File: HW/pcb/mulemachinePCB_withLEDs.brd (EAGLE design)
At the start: 90.2 x 52.1 mm, 29 parts, among them IC1 LD117AV50, IC2 MEGA8-P, J1 DCJ0202, Q1 16Mhz

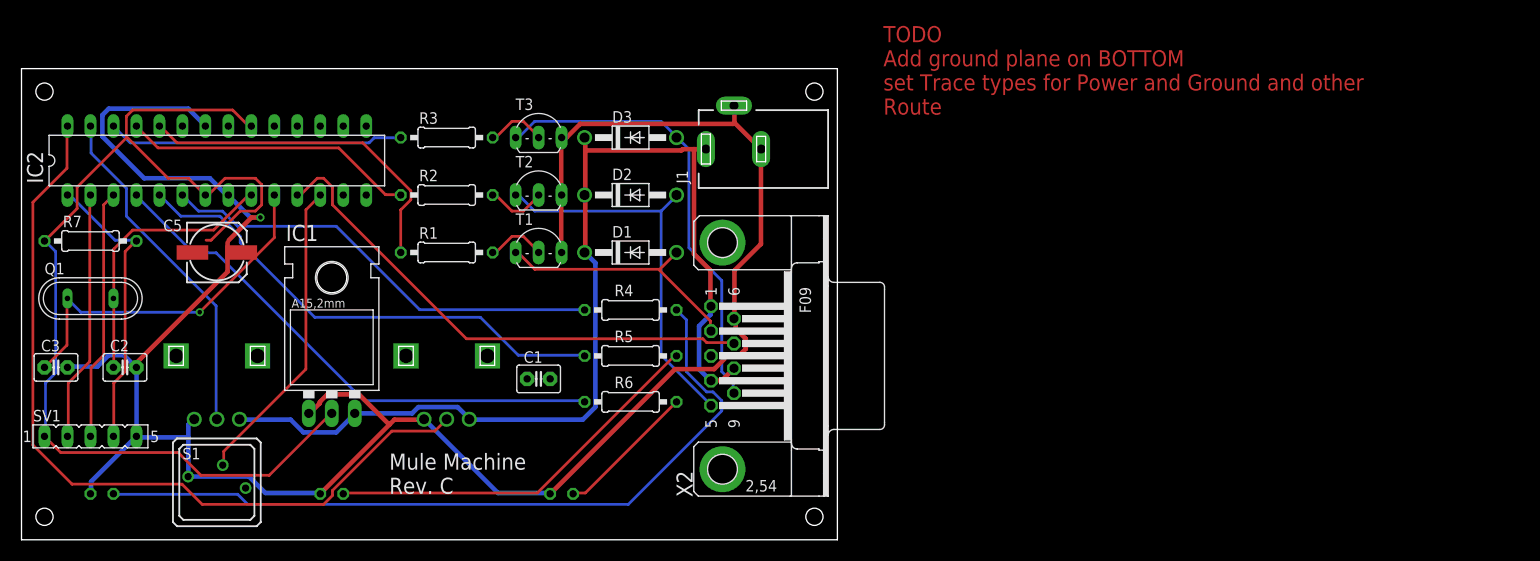
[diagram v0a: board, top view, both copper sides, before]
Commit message: finished layout for PCB. implemented trace widths for PWR and GND. Lined up hole placement to match with Front panel laser design.
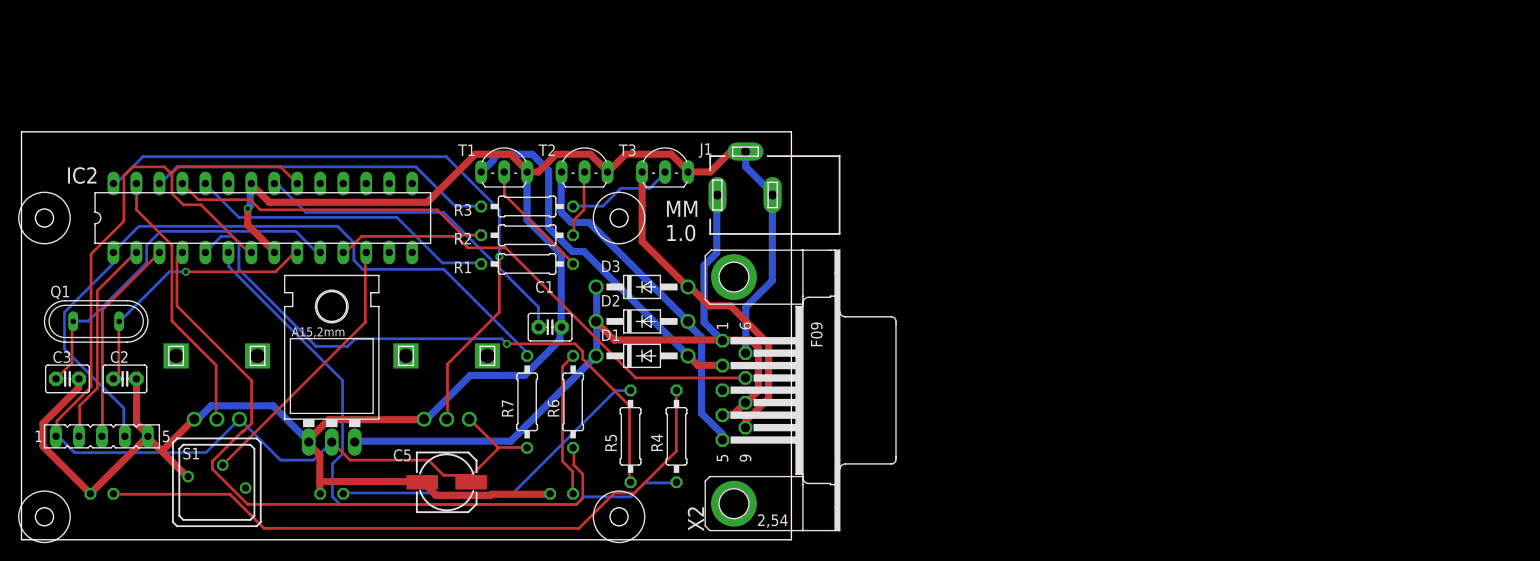
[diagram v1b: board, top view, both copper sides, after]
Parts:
- moved R7 51.4 mm to (55.9, 15.2), turned to 90 degrees
- moved C5 35.9 mm to (47.0, 6.35)
- moved D3 16.6 mm to (68.6, 27.9)
- moved R4 14.9 mm to (72.4, 11.4), turned to 90 degrees
- moved T3 14.5 mm to (71.1, 40.6)
- moved D2 14.0 mm to (68.6, 24.1)
- moved R3 11.7 mm to (55.9, 36.8)
- moved D1 11.5 mm to (68.6, 20.3)
- moved R2 9.94 mm to (55.9, 33.7)
- moved T1 9.67 mm to (53.3, 40.6)
- moved R1 8.98 mm to (55.9, 30.5)
- moved R5 8.89 mm to (67.3, 11.4), turned to 90 degrees
- moved IC2 8.13 mm to (26.7, 35.6)
- moved R6 6.35 mm to (61.0, 15.2), turned to 90 degrees
- moved C1 5.85 mm to (58.4, 23.5)
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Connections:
- net N$7 renamed P1
- net N$8 renamed P2
- net N$9 renamed P3
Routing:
- net RESET: track 32.4 -> 79.6 mm
- net N$13: track 0.00 -> 37.1 mm
- net VCC: track 116.2 -> 84.9 mm
- net N$2: track 49.7 -> 72.1 mm
- net N$4: track 59.1 -> 78.3 mm
- net STRPOT: track 89.5 -> 71.9 mm, vias 0 -> 1
- net P3: track 50.3 -> 36.6 mm
- net P1: track 28.5 -> 40.9 mm
- net 5V: track 120.1 -> 132.4 mm
- net N$3: track 54.8 -> 66.8 mm, vias 0 -> 1
- net N$25: track 85.6 -> 74.1 mm
- net SWTPOT: track 38.2 -> 29.7 mm
- net N$26: track 43.2 -> 36.5 mm
- net N$10: track 6.63 -> 13.3 mm
- net CUPSENSOR: track 57.7 -> 51.7 mm
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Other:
- board size 90.2 x 52.1 mm -> 85.1 x 45.1 mm
- board text added: "G"
- board text added: "MM 1.0"
- board text added: "O"
- board text added: "Y"
- board text removed: "Mule Machine Rev. C"
- board text removed: "TODO Add ground plane on BOTTOM set Trace types for Power and Ground and other Route"

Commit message: ordered MM v1.0 of PCB. Gerber files contained in HW/pcb/mulemachinePCB_withLEDs_2022-02-17.zip
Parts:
- C5: value (none) -> 470uF
- R7: value 200 -> 10k
- moved C1 55.4 mm to (5.71, 40.6)
- moved R7 5.68 mm to (58.4, 20.3)
- moved R6 4.96 mm to (64.8, 12.1)
- moved R5 1.42 mm to (68.6, 12.1)
- moved R4 0.63 mm to (72.4, 12.1)
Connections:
- removed net SWTPOT: IC2.27, R11.2
- new net SOURRPOT: IC2.28, R10.2
- net STRPOT: now also IC2.27, R11.2; no longer IC2.28, R10.2
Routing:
- net SOURRPOT: track 0.00 -> 51.5 mm, vias 0 -> 1
- net STRPOT: track 71.9 -> 29.7 mm, vias 1 -> 0
- net SWTPOT: track 29.7 -> 0.00 mm
- net N$3: track 66.8 -> 88.4 mm, vias 1 -> 0
- net GND: track 240.5 -> 257.9 mm, vias 1 -> 0
- net N$2: track 72.1 -> 83.7 mm
- net RESET: track 79.6 -> 91.1 mm
- net N$13: track 37.1 -> 25.9 mm
- net 5V: track 132.4 -> 139.6 mm
- net N$25: track 74.1 -> 68.2 mm
- net P1: track 40.9 -> 35.6 mm
- net N$27: track 16.2 -> 13.6 mm
- net VCC: track 84.9 -> 86.8 mm
- net N$26: track 36.5 -> 38.0 mm
- net N$4: track 78.3 -> 79.5 mm
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
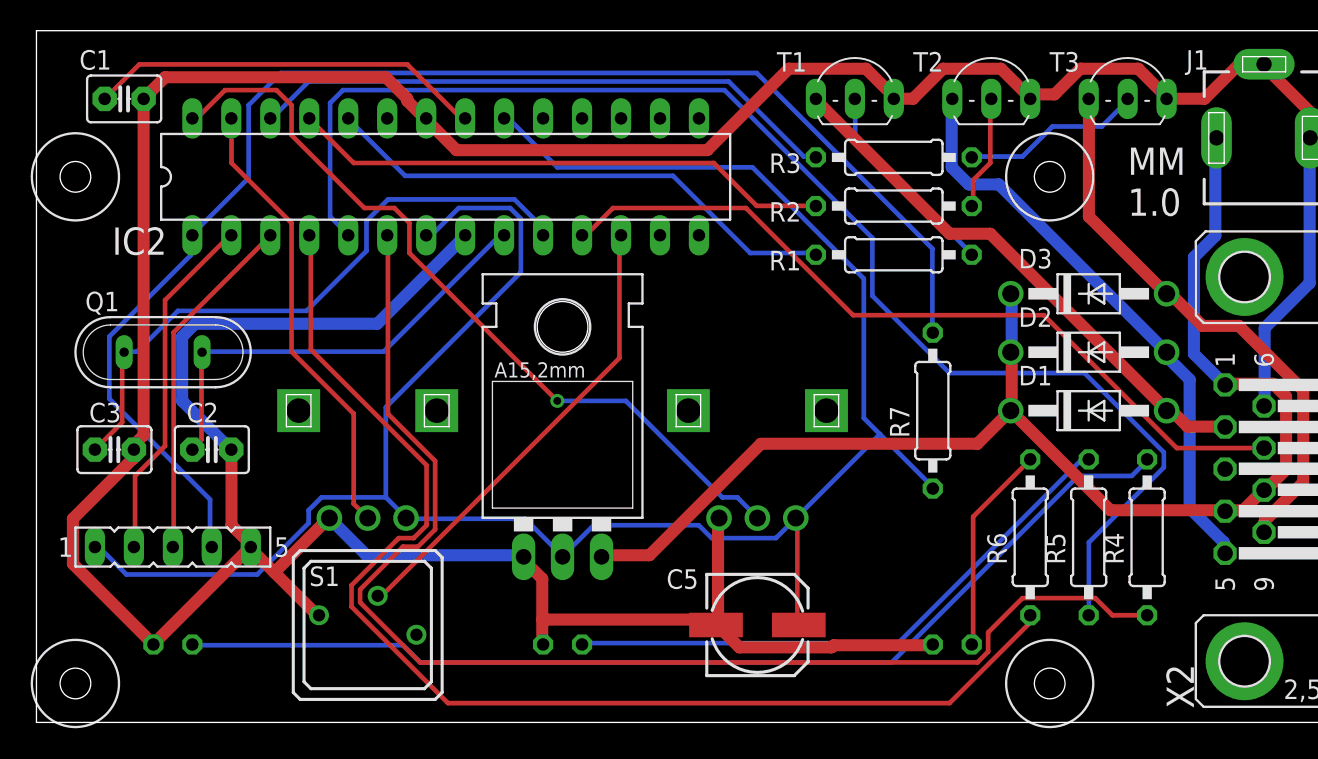
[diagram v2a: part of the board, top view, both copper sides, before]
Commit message: fixed issue #7 on PCB. not yet ordered or tested on physical HW. schematic functionality should not change. just modified capacitor packaging
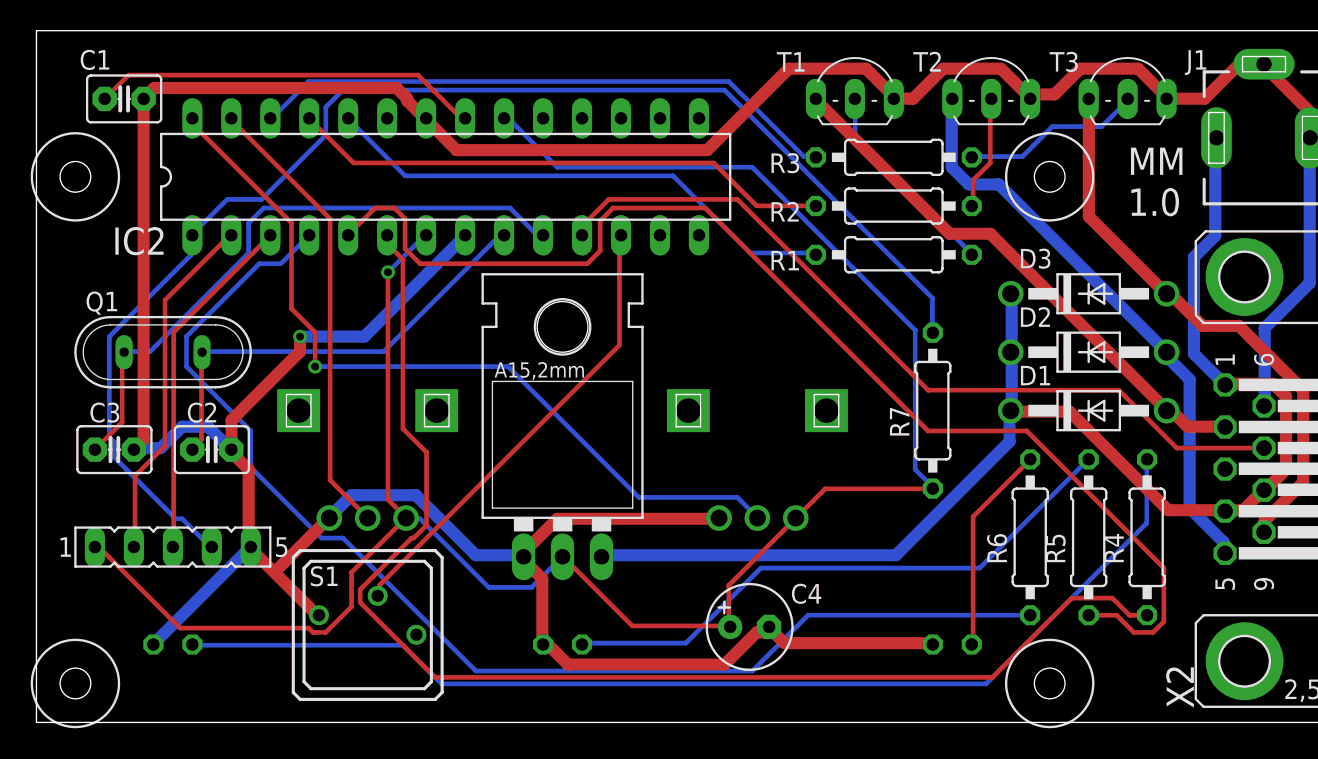
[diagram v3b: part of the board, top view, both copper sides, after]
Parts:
- removed C5: 470uF, rcl:153CLV-0605
- added C4: 470uF, rcl:E2,5-6
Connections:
- net 5V: now also C4.+; no longer C5.+
- net GND: now also C4.-; no longer C5.-
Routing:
- net N$3: track 88.4 -> 78.1 mm
- net GND: track 257.9 -> 250.6 mm, vias 0 -> 1
- net 5V: track 139.6 -> 134.6 mm, vias 0 -> 1
- net RESET: track 91.1 -> 86.8 mm
- net N$25: track 68.2 -> 71.8 mm
- net VCC: track 86.8 -> 87.9 mm
- net SOURRPOT: track 51.5 -> 52.4 mm
- net N$2: track 83.7 -> 82.8 mm
- net CUPSENSOR: track 51.7 -> 52.5 mm
- net N$4: track 79.5 -> 78.8 mm
- net N$11: track 41.0 -> 40.3 mm
- net N$13: track 25.9 -> 25.3 mm
